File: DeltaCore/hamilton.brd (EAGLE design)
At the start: 45 x 41.5 mm, 69 parts, among them Q3 MOSFET-NCHANNEL_SOT23-3, Q4 MOSFET-NCHANNEL_SOT23-3, Q5 MOSFET-NCHANNEL_SOT23-3, Q6 MOSFET-NCHANNEL_SOT23-3, Q7 NFET_AON7408, Q8 NFET_AON7408, U1 SAMR21, U10 PCA9557, U3 MMA7660FC, U4 AT30TS74, U5 MCP73871-2AAI/ML, U7 BQ29718, U8 MCP1824ST-3302E/DB, U9 TPS61090, X1 XTAL

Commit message: todos
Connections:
- removed net LS: U1.9
- net OOB: no longer U1.25
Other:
- board text added: "(route 5V on the 3v3 plane for headers)"
- board text added: "add large vias on the sda/scl line for testing"
- board text added: "can remove 2 100nf caps for hamilton"
- board text added: "check if port expander has slew control"
- board text added: "check inductor is fully shielded"
- board text added: "connect LBO to hamilton, make sure is higher than UVLO"
- board text added: "connect boost EN and i2c port RESET to gpio on hamilton"
- board text added: "connect pads "outside" the chip"
- board text added: "connect the rectified and battery voltage to ADC on hamilton"
- board text added: "double check boost's EN pin"
- board text added: "make battery traces thicker"
- board text added: "move r9,r10 up, add a test point for LBI divider (a via)"
- board text added: "remove pullups on i2c port expander sda/scl"
- board text added: "spread resistors/caps out more to make room for changing"
- board text added: "thicker 5V traces (run along the headers)"
- board text added: "thicker traces on inductor"
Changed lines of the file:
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@@
 <?xml version="1.0" encoding="utf-8"?>
 <!DOCTYPE eagle SYSTEM "eagle.dtd">
-<eagle version="7.6.0">
+<eagle version="7.4.0">
 <drawing>
 <settings>
@@
 <setting verticaltext="up"/>
 </settings>
-<grid distance="10" unitdist="mil" unit="mil" style="lines" multiple="1" display="yes" altdistance="0.000000123031" altunitdist="inch" altunit="inch"/>
+<grid distance="1" unitdist="mm" unit="mm" style="lines" multiple="1" display="yes" altdistance="0.000000123031" altunitdist="inch" altunit="inch"/>
 <layers>
 <layer number="1" name="Top" color="4" fill="1" visible="yes" active="yes"/>
@@
 <layer number="27" name="tValues" color="7" fill="1" visible="no" active="yes"/>
 <layer number="28" name="bValues" color="7" fill="1" visible="no" active="yes"/>
-<layer number="29" name="tStop" color="7" fill="3" visible="no" active="yes"/>
+<layer number="29" name="tStop" color="7" fill="3" visible="yes" active="yes"/>
 <layer number="30" name="bStop" color="7" fill="6" visible="no" active="yes"/>
 <layer number="31" name="tCream" color="7" fill="4" visible="no" active="yes"/>
@@
 <wire x1="12.5" y1="41.5" x2="45" y2="41.5" width="0.4064" layer="20"/>
 <wire x1="45" y1="41.5" x2="45" y2="0" width="0.4064" layer="20"/>
+<text x="19" y="-5" size="1.778" layer="20">spread resistors/caps out more to make room for changing</text>
+<text x="26" y="-3" size="1.778" layer="20">make battery traces thicker</text>
+<text x="18" y="-9" size="1.778" layer="20">connect LBO to hamilton, make sure is higher than UVLO</text>
+<text x="48" y="9" size="1.778" layer="20">move r9,r10 up, add a test point for LBI divider (a via)</text>
+<text x="48" y="6" size="1.778" layer="20">connect pads "outside" the chip</text>
+<text x="48" y="13" size="1.778" layer="20">double check boost's EN pin</text>
+<text x="48" y="17" size="1.778" layer="20">thicker 5V traces (run along the headers)</text>
+<text x="50" y="22" size="1.778" layer="20">(route 5V on the 3v3 plane for headers)</text>
+<text x="49" y="26" size="1.778" layer="20">can remove 2 100nf caps for hamilton</text>
+<text x="49" y="29" size="1.778" layer="20">add large vias on the sda/scl line for testing</text>
+<text x="51" y="33" size="1.778" layer="20">remove pullups on i2c port expander sda/scl</text>
+<text x="49" y="37" size="1.778" layer="20">check if port expander has slew control</text>
+<text x="49" y="40" size="1.778" layer="20">connect boost EN and i2c port RESET to gpio on hamilton</text>
+<text x="49" y="44" size="1.778" layer="20">thicker traces on inductor</text>
+<text x="47" y="2" size="1.778" layer="20">connect the rectified and battery voltage to ADC on hamilton</text>
+<text x="19" y="-13" size="1.778" layer="20">check inductor is fully shielded</text>
 </plain>
 <attributes>
@@
 <wire x1="36.4236" y1="34.9758" x2="36.449" y2="33.5788" width="0.1524" layer="1"/>
 </signal>
-<signal name="LS">
-<contactref element="U1" pad="9"/>
-</signal>
 <signal name="ACC">
 <contactref element="U3" pad="5"/>
@@
 </signal>
 <signal name="OOB">
-<contactref element="U1" pad="25"/>
 <contactref element="U$1" pad="6"/>
-<wire x1="33.058" y1="31.912" x2="32.565" y2="31.912" width="0.1524" layer="1"/>
 <wire x1="32.565" y1="31.912" x2="32.283" y2="32.194" width="0.1524" layer="1"/>
 <wire x1="32.283" y1="32.194" x2="32.283" y2="32.448" width="0.1524" layer="1"/>

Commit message: fixes
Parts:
- removed C13, C7: 100nF, storm:C0402
- added R17: 2k, resistor:R0402
- added R18: 13k, resistor:R0402
- added R19: 5k, resistor:R0402
- R12: value 1.6k -> 10k; device resistor:R0603 -> resistor:R0402
- R13: value 1.6k -> 68k; device resistor:R0603 -> resistor:R0402
- R14: value 1.1k -> 10k
- moved R13 38.3 mm to (43.1, 8.13), turned to 180 degrees
- moved R12 26.9 mm to (30.1, 13.0), turned to 90 degrees
- moved U$2 13.2 mm to (18.2, 14.5)
- moved C20 3.06 mm to (21.5, 10.3)
- moved C5 3.02 mm to (34.4, 40.4)
- moved R5 2.87 mm to (15.4, 1.94)
- moved R11 2.81 mm to (29.3, 15.9), turned to 180 degrees
- moved R10 2.81 mm to (31.1, 8.76)
- moved R14 2.70 mm to (25.1, 38.9), turned to 180 degrees
- moved R6 2.70 mm to (18.3, 1.94)
- moved C19 2.57 mm to (23.2, 6.90), turned to 180 degrees
- moved R15 2.33 mm to (10.0, 1.91)
- moved C3 2.22 mm to (33.9, 24.7)
- moved C15 2.18 mm to (21.5, 2.04)
- moved R7 2.05 mm to (24.3, 2.03)
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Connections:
- removed net N$29: R14.1, U10.P$13
- new net BAT: R18.2, R19.1, U1.9
- new net EN: R12.2, U1.25, U9.EN
- new net N$12: U1.10
- new net N$15: U1.15
- new net N$17: U1.16
- new net N$42: U1.22
- new net RST: R14.1, U1.19, U10.P$13
- new net WIT: R13.1, R17.2, U1.7
- net +3V3: no longer C13.1, C7.1, R12.2, R13.2, R14.2
- net ACC: no longer U1.7
- net GND: now also R12.1, R14.2, R17.1, R19.2; no longer C13.2, C7.2
- net LBO: now also U1.20
- net N$1: now also JP8.1, R13.2, R4.2; no longer R15.2, R4.1, U5.2
- net N$20: now also R18.1
- net RECT: now also R15.2, R4.1, U5.2; no longer JP8.1, R4.2
- net SCL: no longer R12.1
- net SDA: no longer R13.1
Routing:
- net 5V: track 93.5 -> 45.2 mm
- net BAT: track 0.00 -> 47.9 mm, vias 0 -> 2
- net LBO: track 5.15 -> 43.1 mm
- net N$1: track 17.1 -> 54.6 mm, vias 2 -> 1
- net GND: track 210.9 -> 248.2 mm, vias 59 -> 58
- net EN: track 0.00 -> 29.9 mm, vias 0 -> 2
- net WIT: track 0.00 -> 28.3 mm, vias 0 -> 2
- net OOB: track 20.6 -> 0.00 mm, vias 2 -> 0
- net RST: track 0.00 -> 19.3 mm, vias 0 -> 2
- net N$19: track 2.92 -> 20.3 mm, vias 0 -> 2
- net N$20: track 36.9 -> 50.4 mm, vias 2 -> 0
- net +3V3: track 52.8 -> 40.1 mm
- net OUT: track 83.6 -> 71.2 mm, vias 2 -> 4
- net SCL: track 42.6 -> 54.8 mm, vias 2 -> 4
- net ACC: track 10.8 -> 0.00 mm
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- added copper zone on layer 15, net 5V
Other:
- board text added: "move thermistor to a more relevant place"
- board text removed: "double check boost's EN pin"
- board text removed: "make battery traces thicker"
- board text removed: "move r9,r10 up, add a test point for LBI divider (a via)"

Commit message: more
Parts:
- moved C11 0.79 mm to (28.6, 35.6)
- renumbered U$2 to RT1
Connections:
- removed net ACC: U3.5
- removed net OOB: U$1.6
- removed net SD: U1.27
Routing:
- net SCL: track 54.8 -> 55.7 mm
- net N$1: track 54.6 -> 53.9 mm
- net BAT: track 47.9 -> 48.6 mm
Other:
- board text added: "5V"
- board text added: "D25"
- board text added: "G Fierro"
- board text added: "GND"
- board text added: "LBI"
- board text added: "MP Andersen"
- board text added: "Q7"
- board text added: "Q8"
- board text added: "SCL"
- board text added: "SDA"
- board text added: "UC Berkeley"
- board text removed: "(route 5V on the 3v3 plane for headers)"
- board text removed: "add large vias on the sda/scl line for testing"
- board text removed: "can remove 2 100nf caps for hamilton"
- board text removed: "check if port expander has slew control"
- board text removed: "check inductor is fully shielded"
- board text removed: "connect LBO to hamilton, make sure is higher than UVLO"
- board text removed: "connect boost EN and i2c port RESET to gpio on hamilton"
- board text removed: "connect pads "outside" the chip"
- board text removed: "connect the rectified and battery voltage to ADC on hamilton"
- board text removed: "move thermistor to a more relevant place"
- board text removed: "remove pullups on i2c port expander sda/scl"
- board text removed: "spread resistors/caps out more to make room for changing"
- board text removed: "thicker 5V traces (run along the headers)"
- board text removed: "thicker traces on inductor"

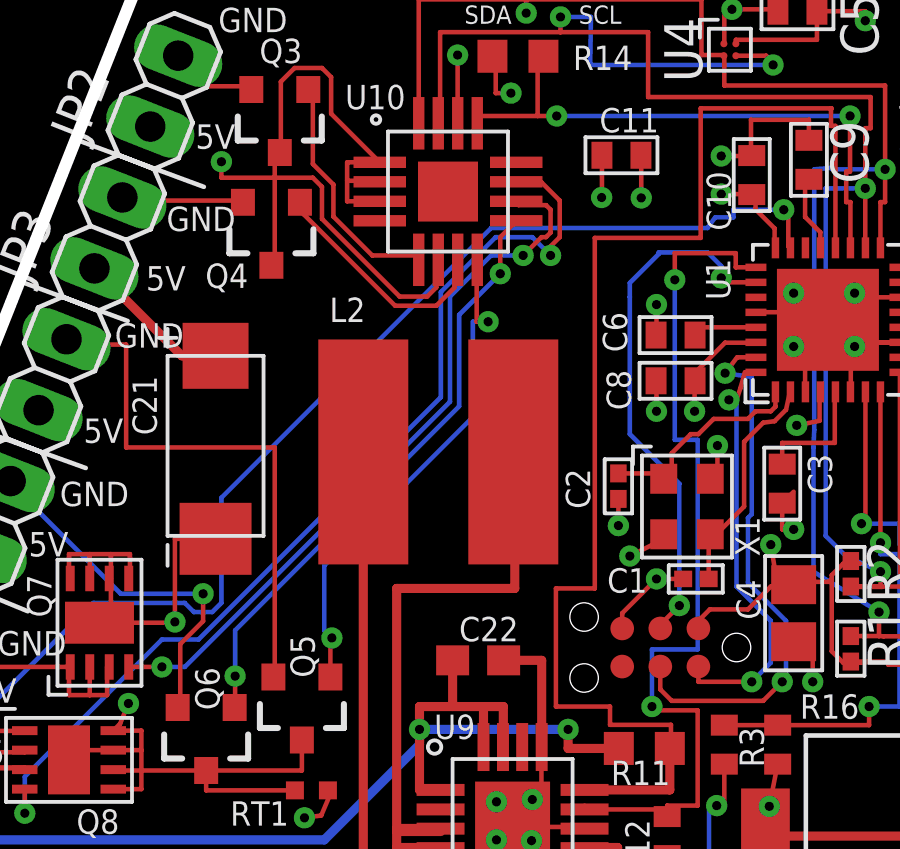
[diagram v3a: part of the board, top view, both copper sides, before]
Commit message: move i2c out from under inductor
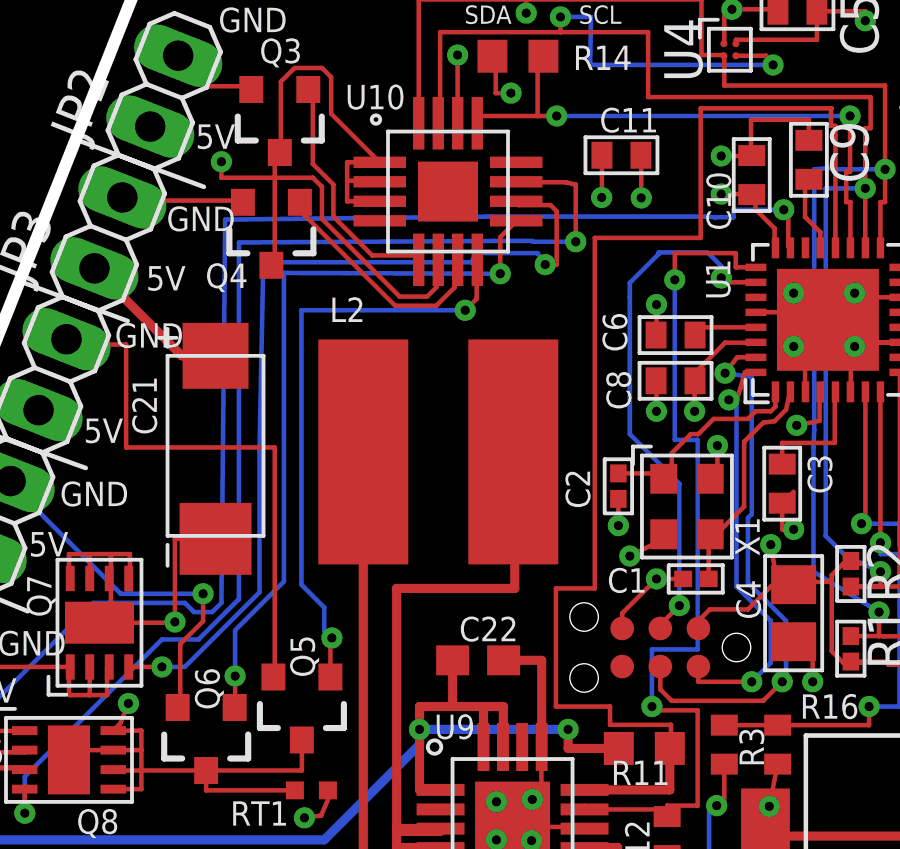
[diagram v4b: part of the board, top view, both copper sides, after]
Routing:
- net N$40: track 24.2 -> 29.8 mm
- net N$41: track 33.0 -> 38.6 mm
- net D25: track 41.0 -> 46.2 mm
- net N$33: track 20.1 -> 24.4 mm
- net N$32: track 17.0 -> 20.0 mm
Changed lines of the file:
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@@
 <setting verticaltext="up"/>
 </settings>
-<grid distance="1" unitdist="mil" unit="mil" style="lines" multiple="1" display="yes" altdistance="0.000000123031" altunitdist="inch" altunit="inch"/>
+<grid distance="5" unitdist="mil" unit="mil" style="lines" multiple="1" display="yes" altdistance="0.000000123031" altunitdist="inch" altunit="inch"/>
 <layers>
 <layer number="1" name="Top" color="4" fill="1" visible="yes" active="yes"/>
@@
 <contactref element="U10" pad="P$8"/>
 <wire x1="23.7682" y1="32.1636" x2="23.749" y2="32.1636" width="0.1524" layer="1"/>
-<wire x1="23.749" y1="32.1636" x2="23.749" y2="30.099" width="0.1524" layer="1"/>
-<wire x1="23.749" y1="30.099" x2="24.13" y2="30.099" width="0.1524" layer="1"/>
-<via x="24.13" y="30.099" extent="1-16" drill="0.3048"/>
-<wire x1="24.13" y1="30.099" x2="23.622" y2="30.099" width="0.1524" layer="16"/>
-<wire x1="23.622" y1="30.099" x2="23.622" y2="26.924" width="0.1524" layer="16"/>
-<wire x1="23.622" y1="26.924" x2="18.669" y2="21.971" width="0.1524" layer="16"/>
-<wire x1="18.669" y1="21.971" x2="18.669" y2="19.812" width="0.1524" layer="16"/>
+<wire x1="18.669" y1="20.574" x2="18.669" y2="19.812" width="0.1524" layer="16"/>
 <wire x1="18.669" y1="19.812" x2="18.923" y2="19.558" width="0.1524" layer="16"/>
 <via x="18.923" y="19.558" extent="1-16" drill="0.3048"/>
 <wire x1="18.923" y1="19.558" x2="18.873" y2="19.508" width="0.1524" layer="1"/>
 <wire x1="18.873" y1="19.508" x2="18.873" y2="18.256" width="0.1524" layer="1"/>
+<wire x1="23.749" y1="32.1636" x2="23.749" y2="30.861" width="0.1524" layer="1"/>
+<wire x1="23.749" y1="30.861" x2="23.368" y2="30.48" width="0.1524" layer="1"/>
+<via x="23.368" y="30.48" extent="1-16" drill="0.3048"/>
+<wire x1="23.368" y1="30.48" x2="17.907" y2="30.48" width="0.1524" layer="16"/>
+<wire x1="17.907" y1="30.48" x2="17.907" y2="21.336" width="0.1524" layer="16"/>
+<wire x1="17.907" y1="21.336" x2="18.669" y2="20.574" width="0.1524" layer="16"/>
 </signal>
 <signal name="N$33">
@@
 <wire x1="15.6972" y1="18.288" x2="15.6972" y2="17.3736" width="0.1524" layer="1"/>
 <wire x1="15.6972" y1="19.812" x2="15.6972" y2="18.288" width="0.1524" layer="16"/>
-<wire x1="23.1648" y1="27.2796" x2="15.6972" y2="19.812" width="0.1524" layer="16"/>
-<wire x1="23.1648" y1="30.3276" x2="23.1648" y2="27.2796" width="0.1524" layer="16"/>
-<wire x1="24.5364" y1="31.6992" x2="23.1648" y2="30.3276" width="0.1524" layer="16"/>
+<wire x1="24.5364" y1="31.6992" x2="17.3228" y2="31.7246" width="0.1524" layer="16"/>
 <wire x1="24.5364" y1="32.9184" x2="24.5364" y2="31.6992" width="0.1524" layer="1"/>
 <wire x1="24.9936" y1="33.3756" x2="24.5364" y2="32.9184" width="0.1524" layer="1"/>
@@
 <via x="15.6972" y="18.288" extent="1-16" drill="0.3048"/>
 <via x="24.5364" y="31.6992" extent="1-16" drill="0.3048"/>
+<wire x1="17.3228" y1="31.7246" x2="17.3228" y2="21.4376" width="0.1524" layer="16"/>
+<wire x1="17.3228" y1="21.4376" x2="15.6972" y2="19.812" width="0.1524" layer="16"/>
 </signal>
 <signal name="N$14">
@@
 <wire x1="33.9852" y1="33.8328" x2="34.1376" y2="33.6804" width="0.1524" layer="1"/>
 <wire x1="32.3088" y1="33.8328" x2="33.9852" y2="33.8328" width="0.1524" layer="16"/>
-<wire x1="24.2316" y1="33.2232" x2="31.4452" y2="33.2232" width="0.1524" layer="16"/>
-<wire x1="15.24" y1="24.2316" x2="24.2316" y2="33.2232" width="0.1524" layer="16"/>
-<wire x1="15.24" y1="20.7264" x2="15.24" y2="24.2316" width="0.1524" layer="16"/>
+<wire x1="24.2316" y1="33.6042" x2="31.4452" y2="33.6042" width="0.1524" layer="16"/>
+<wire x1="15.367" y1="33.5026" x2="24.2316" y2="33.6042" width="0.1524" layer="16"/>
+<wire x1="15.24" y1="20.7264" x2="15.367" y2="33.5026" width="0.1524" layer="16"/>
 <wire x1="14.9352" y1="20.4216" x2="15.24" y2="20.7264" width="0.1524" layer="16"/>
 <wire x1="14.3256" y1="20.4216" x2="14.9352" y2="20.4216" width="0.1524" layer="16"/>
@@
 <wire x1="32.3088" y1="33.8328" x2="32.3088" y2="33.5788" width="0.1524" layer="16"/>
 <wire x1="32.3088" y1="33.5788" x2="31.6992" y2="33.5788" width="0.1524" layer="16"/>
-<wire x1="31.6992" y1="33.5788" x2="31.4452" y2="33.2232" width="0.1524" layer="16"/>
+<wire x1="31.6992" y1="33.5788" x2="31.4452" y2="33.6042" width="0.1524" layer="16"/>
 </signal>
 <signal name="N$37">
@@
 <wire x1="13.2588" y1="18.5928" x2="12.192" y2="18.5928" width="0.1524" layer="1"/>
 <wire x1="14.0208" y1="18.5928" x2="13.2588" y2="18.5928" width="0.1524" layer="16"/>
-<wire x1="22.86" y1="27.432" x2="14.0208" y2="18.5928" width="0.1524" layer="16"/>
-<wire x1="22.86" y1="30.9372" x2="22.86" y2="27.432" width="0.1524" layer="16"/>
-<wire x1="24.2316" y1="32.3088" x2="22.86" y2="30.9372" width="0.1524" layer="16"/>
-<wire x1="25.2984" y1="32.3088" x2="24.2316" y2="32.3088" width="0.1524" layer="16"/>
-<wire x1="25.908" y1="32.9184" x2="25.2984" y2="32.3088" width="0.1524" layer="1"/>
-<wire x1="26.0604" y1="32.9184" x2="25.908" y2="32.9184" width="0.1524" layer="1"/>
-<wire x1="26.2128" y1="33.0708" x2="26.0604" y2="32.9184" width="0.1524" layer="1"/>
-<wire x1="26.2128" y1="33.8328" x2="26.2128" y2="33.0708" width="0.1524" layer="1"/>
-<wire x1="26.0604" y1="33.9852" x2="26.2128" y2="33.8328" width="0.1524" layer="1"/>
-<wire x1="25.146" y1="33.9852" x2="26.0604" y2="33.9852" width="0.1524" layer="1"/>
+<wire x1="16.637" y1="32.0802" x2="16.51" y2="25.781" width="0.1524" layer="16"/>
 <wire x1="12.192" y1="18.5928" x2="12.151" y2="18.591" width="0.1524" layer="1"/>
 <wire x1="25.146" y1="33.9852" x2="25.0682" y2="34.1136" width="0.1524" layer="1"/>
 <via x="13.2588" y="18.5928" extent="1-16" drill="0.3048"/>
-<via x="25.2984" y="32.3088" extent="1-16" drill="0.3048"/>
+<wire x1="16.51" y1="25.781" x2="16.51" y2="21.082" width="0.1524" layer="16"/>
+<wire x1="16.51" y1="21.082" x2="14.0208" y2="18.5928" width="0.1524" layer="16"/>
+<wire x1="25.146" y1="33.9852" x2="26.2128" y2="33.9852" width="0.1524" layer="1"/>
+<wire x1="26.2128" y1="33.9852" x2="26.416" y2="33.782" width="0.1524" layer="1"/>
+<wire x1="26.416" y1="33.782" x2="26.416" y2="32.004" width="0.1524" layer="1"/>
+<wire x1="26.416" y1="32.004" x2="26.035" y2="32.004" width="0.1524" layer="1"/>
+<via x="26.035" y="32.004" extent="1-16" drill="0.3048"/>
+<wire x1="16.637" y1="32.0802" x2="23.5712" y2="32.0802" width="0.1524" layer="16"/>
+<wire x1="23.5712" y1="32.0802" x2="23.749" y2="32.385" width="0.1524" layer="16"/>
+<wire x1="23.749" y1="32.385" x2="25.781" y2="32.385" width="0.1524" layer="16"/>
+<wire x1="25.781" y1="32.385" x2="26.035" y2="32.004" width="0.1524" layer="16"/>
 </signal>
 <signal name="N$41">
@@
 <wire x1="13.2588" y1="19.5072" x2="8.6868" y2="14.9352" width="0.1524" layer="16"/>
 <wire x1="14.478" y1="19.5072" x2="13.2588" y2="19.5072" width="0.1524" layer="16"/>
-<wire x1="22.5552" y1="27.5844" x2="14.478" y2="19.5072" width="0.1524" layer="16"/>
-<wire x1="22.5552" y1="31.0896" x2="22.5552" y2="27.5844" width="0.1524" layer="16"/>
-<wire x1="24.384" y1="32.9184" x2="22.5552" y2="31.0896" width="0.1524" layer="16"/>
-<wire x1="25.6032" y1="32.9184" x2="24.384" y2="32.9184" width="0.1524" layer="16"/>
-<wire x1="26.2128" y1="32.3088" x2="25.6032" y2="32.9184" width="0.1524" layer="16"/>
-<wire x1="26.2128" y1="32.6136" x2="26.2128" y2="32.3088" width="0.1524" layer="1"/>
-<wire x1="26.5176" y1="32.9184" x2="26.2128" y2="32.6136" width="0.1524" layer="1"/>
-<wire x1="26.5176" y1="34.1376" x2="26.5176" y2="32.9184" width="0.1524" layer="1"/>
-<wire x1="25.908" y1="34.7472" x2="26.5176" y2="34.1376" width="0.1524" layer="1"/>
-<wire x1="25.146" y1="34.7472" x2="25.908" y2="34.7472" width="0.1524" layer="1"/>
+<wire x1="24.384" y1="32.7914" x2="15.8242" y2="32.7406" width="0.1524" layer="16"/>
+<wire x1="25.6032" y1="32.7914" x2="24.384" y2="32.7914" width="0.1524" layer="16"/>
 <wire x1="8.6868" y1="14.478" x2="8.685" y2="14.519" width="0.1524" layer="1"/>
 <wire x1="25.146" y1="34.7472" x2="25.0682" y2="34.7636" width="0.1524" layer="1"/>
 <via x="8.6868" y="13.716" extent="1-16" drill="0.3048"/>
-<via x="26.2128" y="32.3088" extent="1-16" drill="0.3048"/>
+<wire x1="15.8242" y1="32.7406" x2="15.8242" y2="20.8534" width="0.1524" layer="16"/>
+<wire x1="15.8242" y1="20.8534" x2="14.478" y2="19.5072" width="0.1524" layer="16"/>
+<wire x1="25.146" y1="34.7472" x2="26.7208" y2="34.7472" width="0.1524" layer="1"/>
+<wire x1="26.7208" y1="34.7472" x2="27.051" y2="34.671" width="0.1524" layer="1"/>
+<wire x1="27.051" y1="34.671" x2="27.051" y2="32.766" width="0.1524" layer="1"/>
+<via x="27.051" y="32.766" extent="1-16" drill="0.3048"/>
+<wire x1="27.051" y1="32.766" x2="25.6286" y2="32.766" width="0.1524" layer="16"/>
+<wire x1="25.6286" y1="32.766" x2="25.6032" y2="32.7914" width="0.1524" layer="16"/>
 </signal>
 <signal name="RECT">
